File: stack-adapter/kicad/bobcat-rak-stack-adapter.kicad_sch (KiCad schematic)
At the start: 17 parts, among them J1 PCIE-52P52H

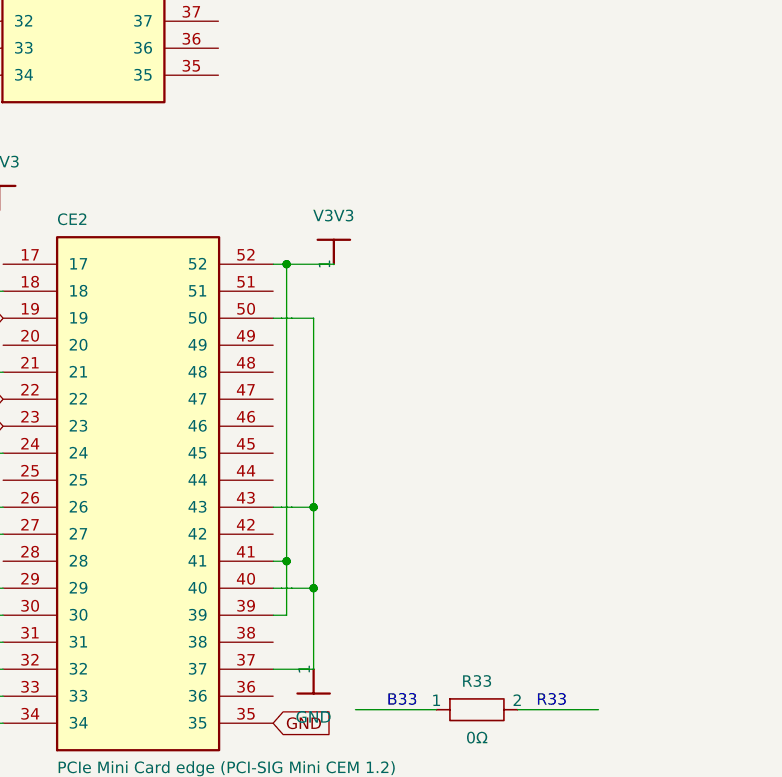
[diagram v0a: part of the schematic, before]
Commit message: stack-adapter: GPS PPS to the processor (R47P fitted: RAK 19 -> finger 47 -> GPIO4_D0); docs: PPS/UART/qErr notes
Adapter: R47P 0R fitted, R45P (-> finger 45 / GPIO4_C7), R19, R23, R30-R33 DNP. Fingers 45/47 are their own
nets; the RAK's 45/47 come only from the SPI reroute of Bobcat 3/5. KiCad DRC 0 errors / 0 unconnected.
New docs/pps-uart-qerr.md: PPS path and core-3 capture, IO-voltage evidence, the GPS UART on RAK 31/33
(unmapped) with mapping method and fallback, and qErr (UBX-TIM-TP) sawtooth correction incl. the SX1303
latch and mandatory UBX checksum verification.

Co-Authored-By: Claude Opus 5.5 <noreply@anthropic.com>
Claude-Session: https://claude.ai/code/session_01Au7yLXRzrrweJwAkfxbhgS
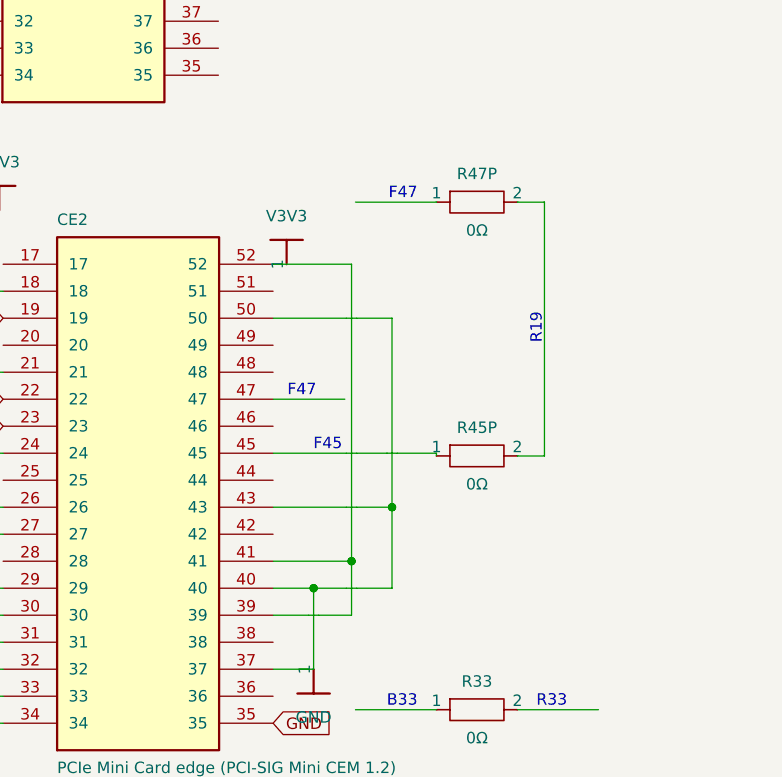
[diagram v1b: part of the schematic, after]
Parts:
- removed GND (x4): GND, symbol Custom:rail_down
- removed V3V3 (x4): V3V3, symbol Custom:rail_up
- added GND (x4): GND, symbol Custom:rail_down
- added R45P, R47P: 0Ω, symbol Device:boxresistor_right
- added V3V3 (x4): V3V3, symbol Custom:rail_up
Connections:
- net at CE2.18, CE2.21, CE2.26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: now also GND.1
- net at CE2.24, J1.39, J1.41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: now also V3V3.1
- net at CE2.37, CE2.40, CE2.43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: now also GND.1
- net at CE2.45: now also R45P.1
- net at CE1.23, J1.2: now also V3V3.1
- net at CE1.40, CE1.46: now also GND.1
- net at J1.24: now also V3V3.1
- net at CE1.25: now also GND.1
- new net: R45P.2, R47P.2
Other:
- note added: "F45"
- note added: "F47"
